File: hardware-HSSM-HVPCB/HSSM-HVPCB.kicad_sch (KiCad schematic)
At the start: 16 parts, among them J1 2086-1103, J2 2601-1110, K1 G6DN-1A-L DC12, K2 G6DN-1A-L DC12, U1 LNK3202D-TL, U2 CS5480-INZ

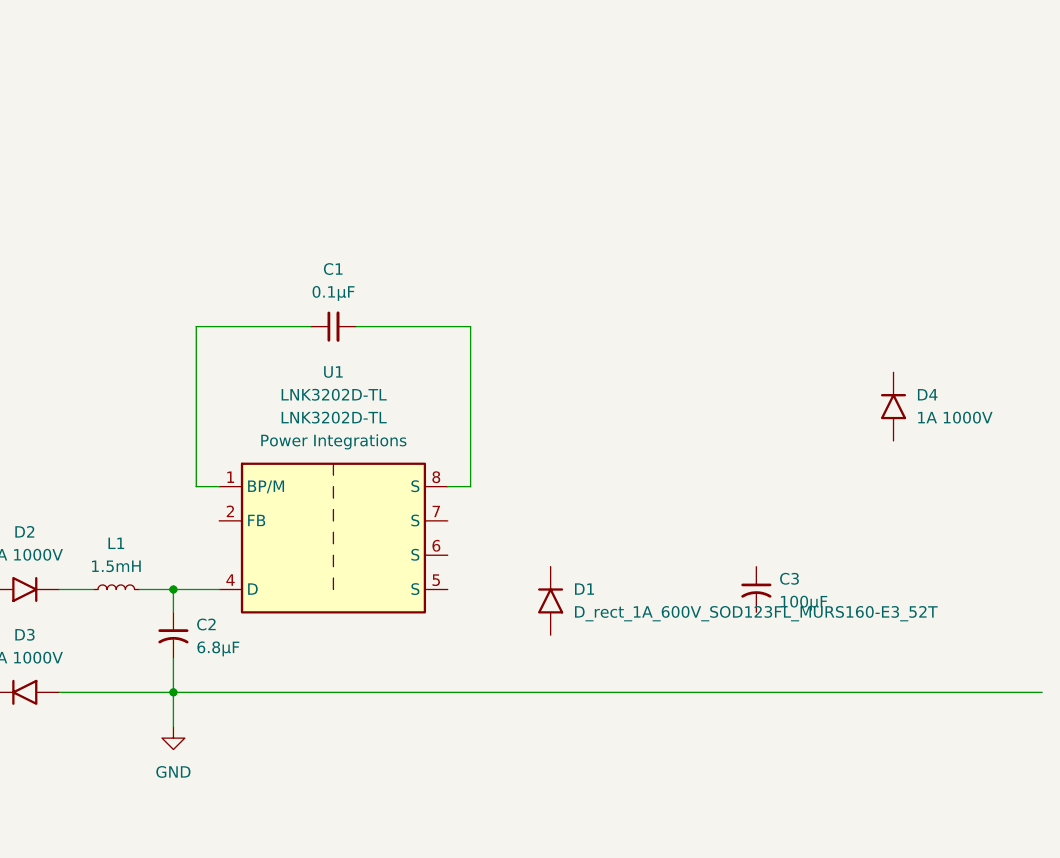
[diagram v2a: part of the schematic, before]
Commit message: [#3] SCH LNK3204 connections WIP
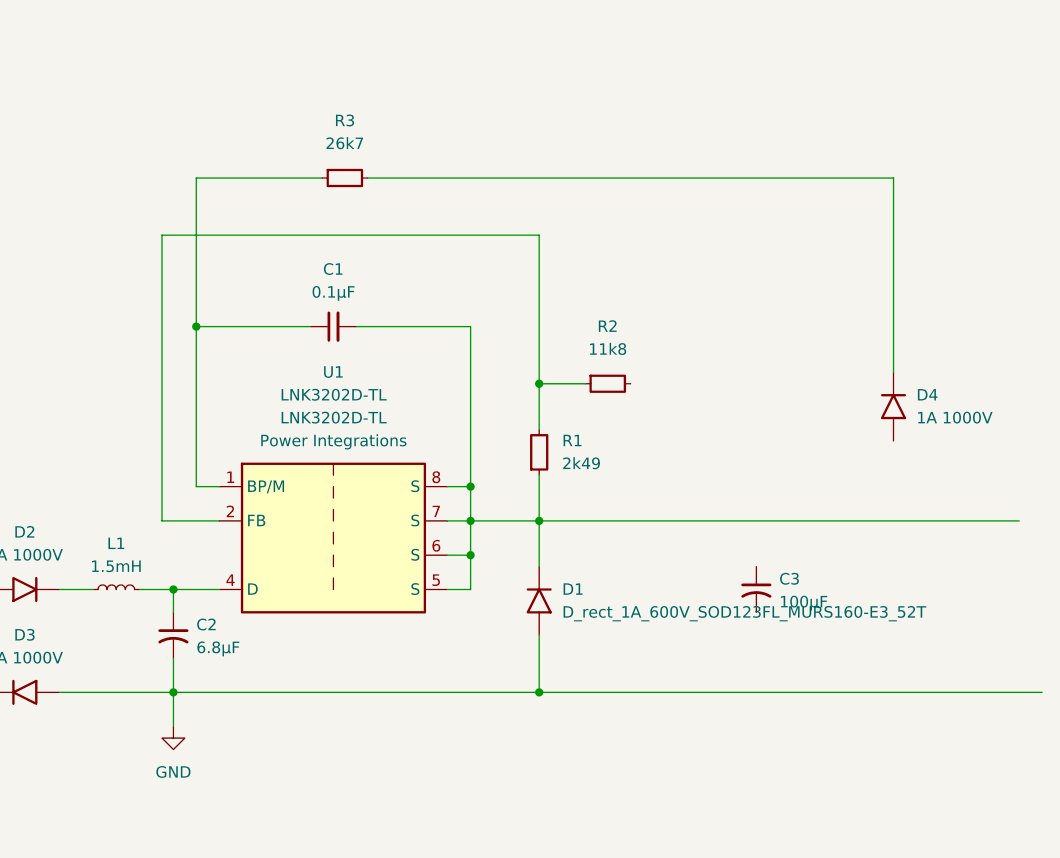
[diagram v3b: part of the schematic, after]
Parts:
- added R1: R_2k49_1pct_0402_RC0402FR-072K49L, HSSM-HVPCB:R_0402, symbol HSSM-HVPCB:R_2k49_1pct_0402_RC0402FR-072K49L
- added R2: R_11k8_1pct_0402_RC0402FR-0711K8L, HSSM-HVPCB:R_0402, symbol HSSM-HVPCB:R_11k8_1pct_0402_RC0402FR-0711K8L
- added R3: R_26k7_0.1pct_0402_CPF0402B26K7E1, HSSM-HVPCB:R_0402, symbol HSSM-HVPCB:R_26k7_0.1pct_0402_CPF0402B26K7E1
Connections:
- net GND: now also D1.2 (A)
- net at D1.1 (K): now also C1.2, U1.5 (S), U1.6 (S), U1.7 (S), U1.8 (S), R1.1
- net at D4.1 (K): now also R3.2
- net at C1.1, U1.1 (BP/M): now also R3.1
- net at U1.2 (FB): now also R1.2, R2.1
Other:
- moved on the sheet: D1

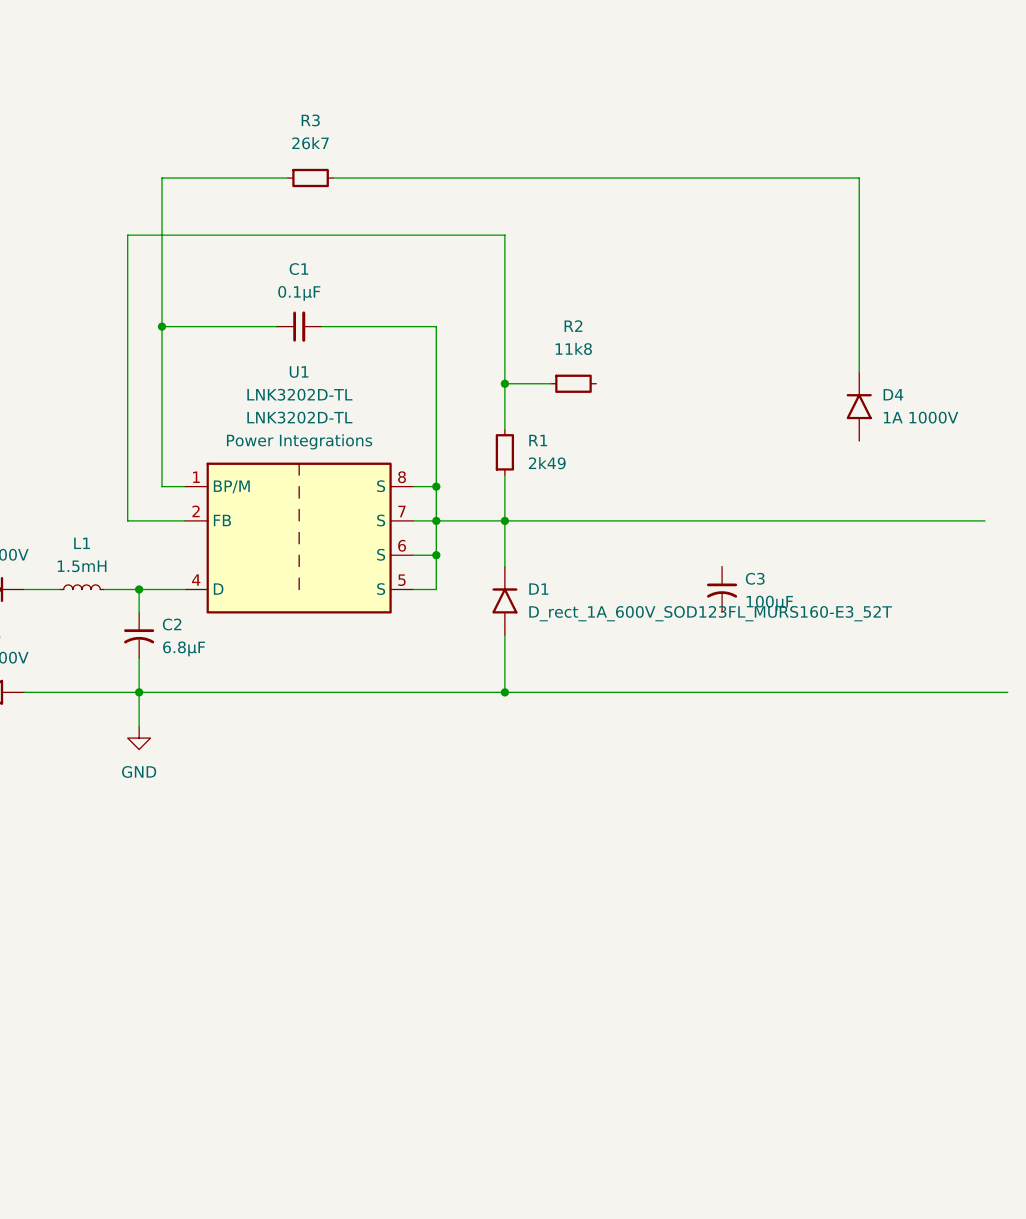
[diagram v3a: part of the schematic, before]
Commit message: [#3] SCH LNK3204 connections WIP
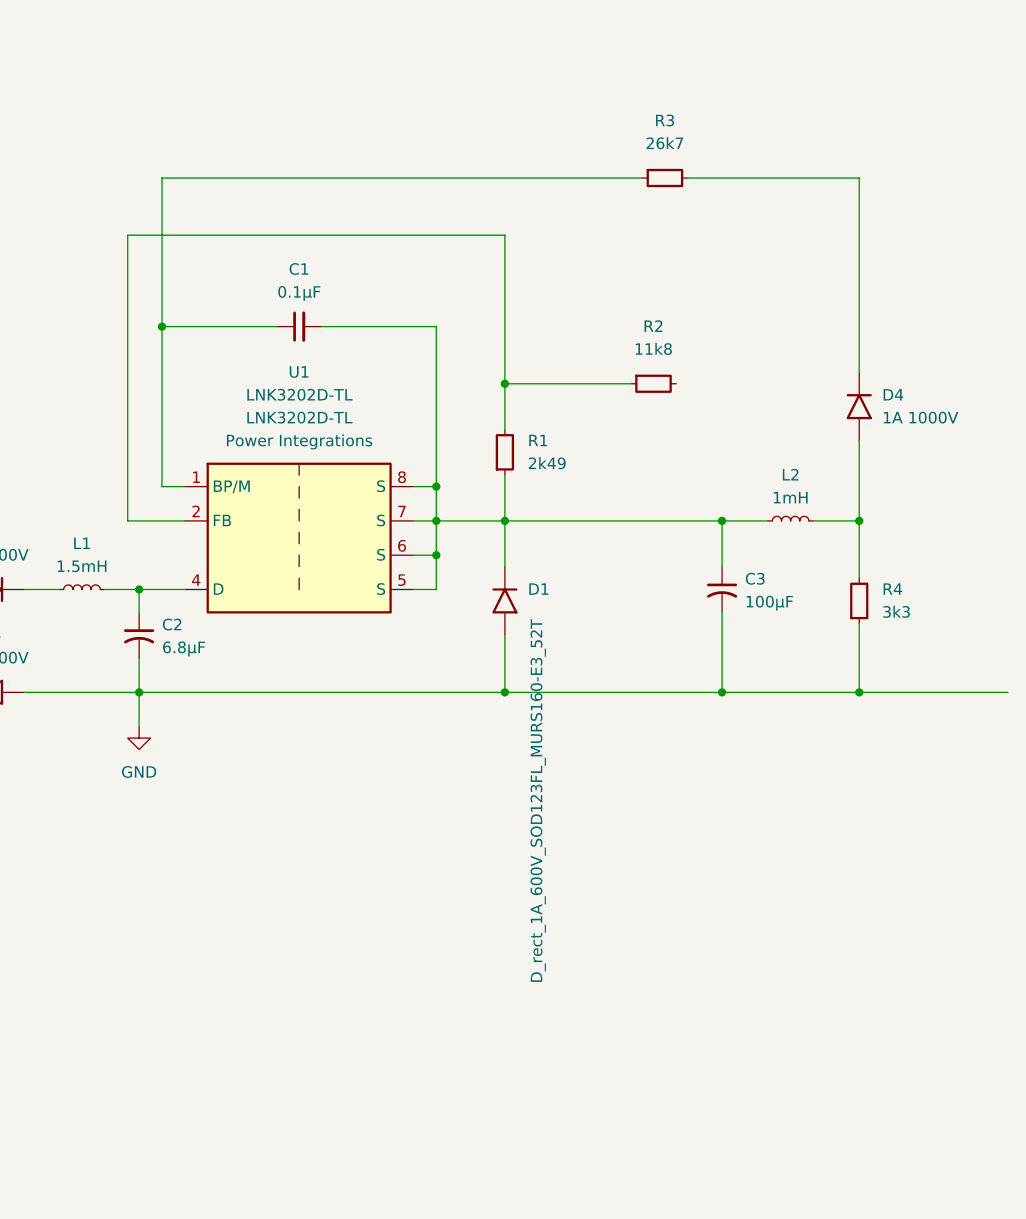
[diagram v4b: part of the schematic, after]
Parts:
- added L2: L_1mH_10pct_SDR0503-102KL, HSSM-HVPCB:L_SMD_5x5mm, symbol HSSM-HVPCB:L_1mH_10pct_SDR0503-102KL
- added R4: R_3k3_5pct_0402_RC0402JR-073K3L, HSSM-HVPCB:R_0402, symbol HSSM-HVPCB:R_3k3_5pct_0402_RC0402JR-073K3L
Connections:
- net GND: now also C3.2, R4.1
- net at C1.2, D1.1 (K), R1.1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: now also C3.1, L2.1
- net at D4.2 (A): now also L2.2, R4.2
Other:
- moved on the sheet: R2, R3

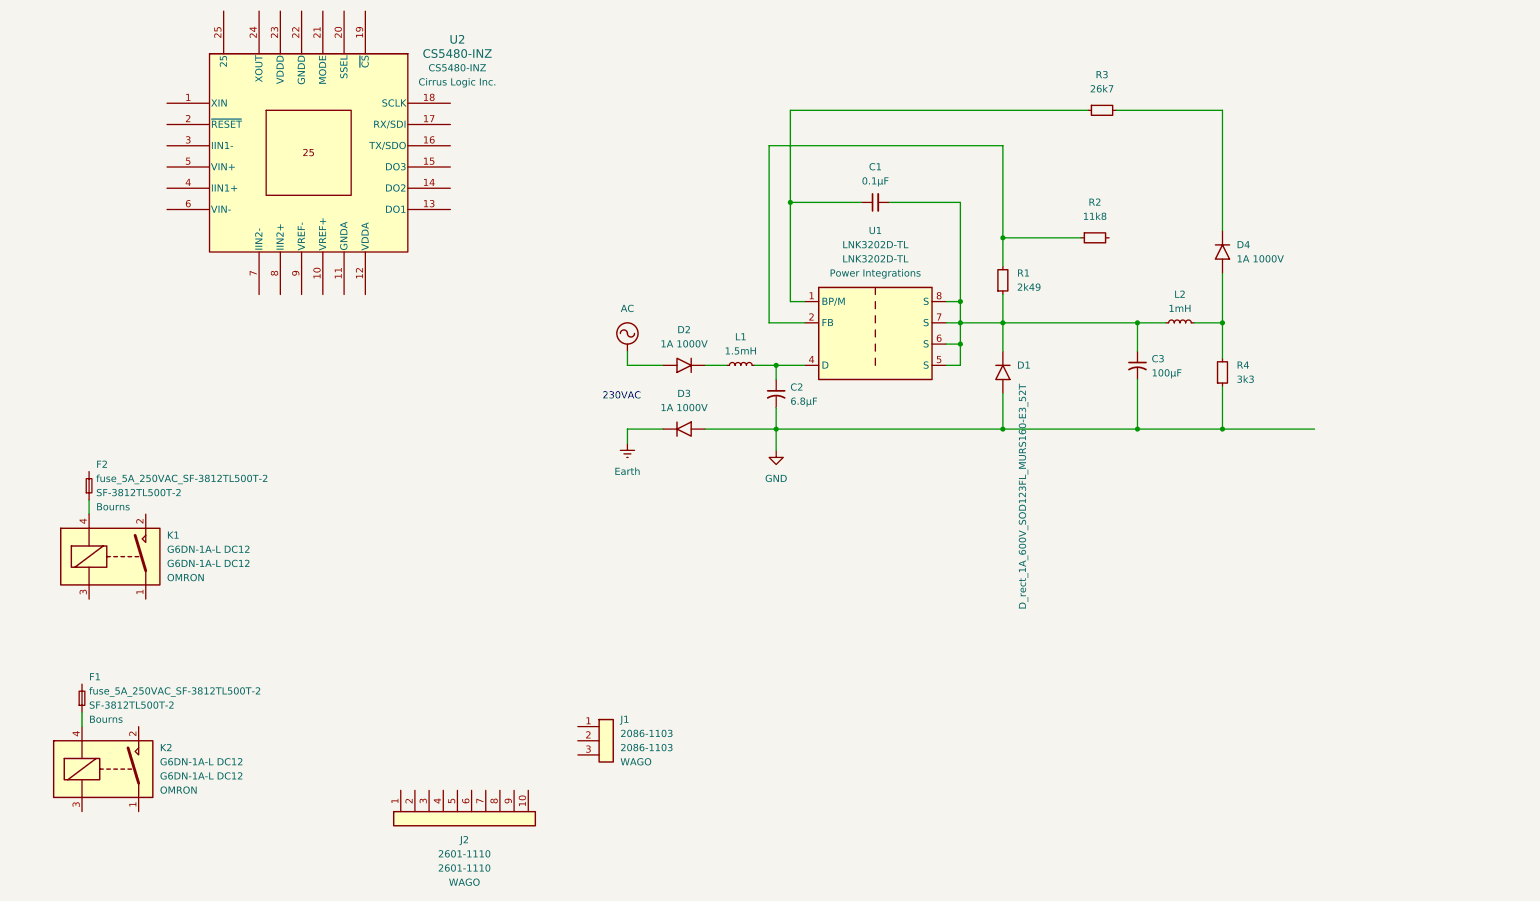
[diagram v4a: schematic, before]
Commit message: [#3] SCH LNK3204 connections
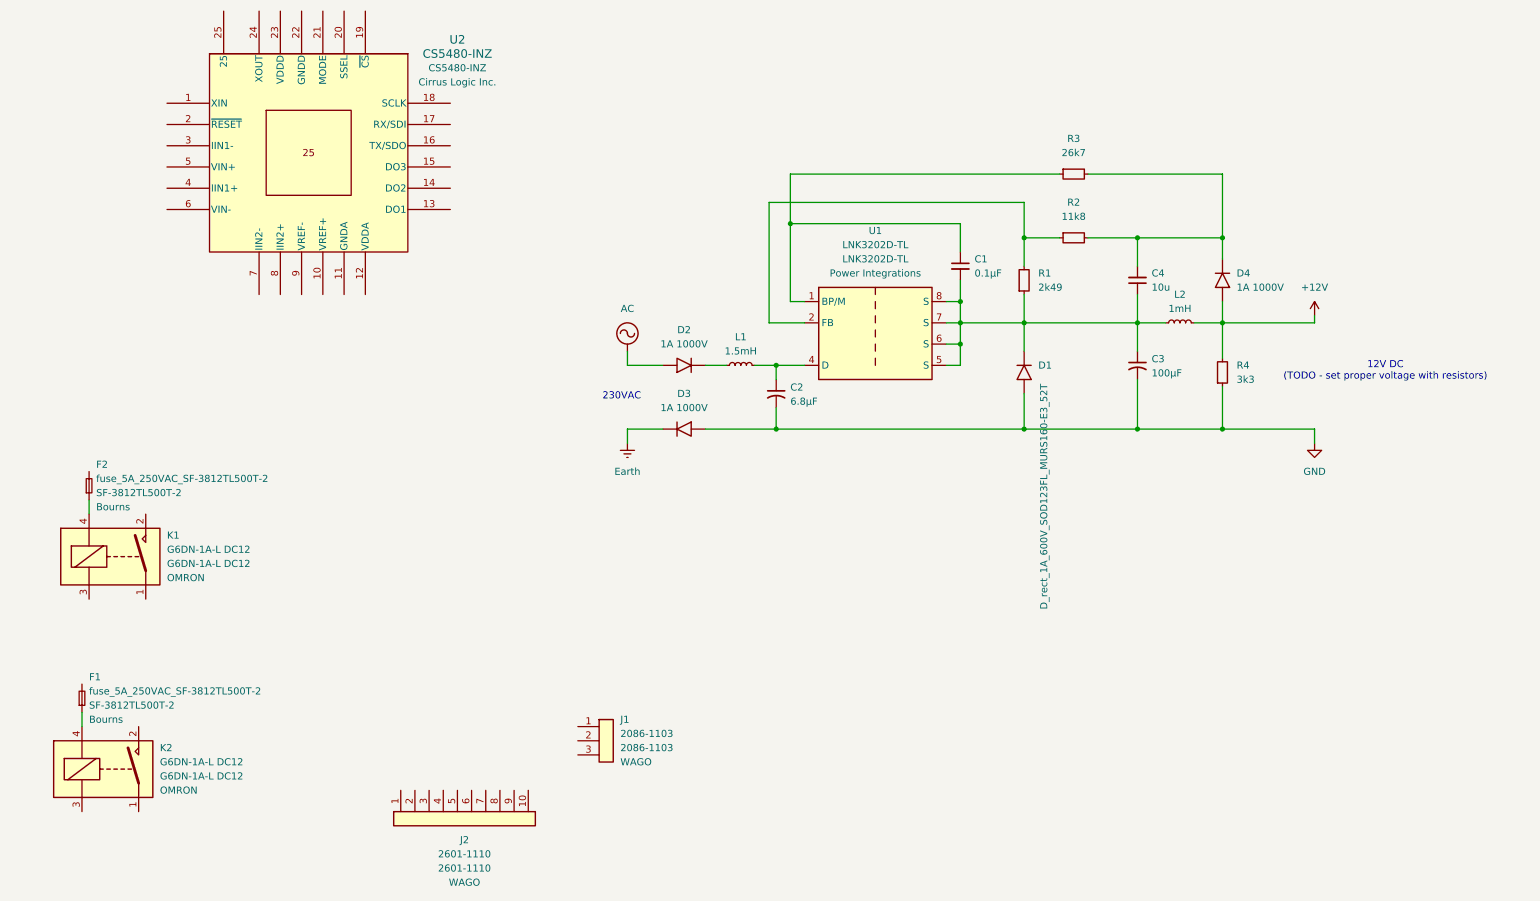
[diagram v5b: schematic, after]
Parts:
- added C4: C_10u_10pct_25V_0603_GRM188R61E106KA73D, HSSM-HVPCB:C_0603, symbol HSSM-HVPCB:C_10u_10pct_25V_0603_GRM188R61E106KA73D
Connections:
- net at C1.2, C3.1, D1.1 (K)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: now also C4.1
- net at D4.1 (K), R3.2: now also R2.2, C4.2
- net +12V: now reaches D4.2 (A), L2.2, R4.2
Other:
- note added: "12V DC (TODO - set proper voltage with resistors)"
- moved on the sheet: C1, D1, D4, R1, R2, R3
